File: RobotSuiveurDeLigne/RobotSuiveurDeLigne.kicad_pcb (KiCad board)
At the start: 2 copper layers, 108 x 48 mm, 22 parts, among them J1 US_IUT_VdA, J2 Conn_02x05_Odd_Even, U1 CNY70_IUT_VdA, U2 CNY70_IUT_VdA, U3 CNY70_IUT_VdA, U4 CNY70_IUT_VdA, U5 CNY70_IUT_VdA, U6 CNY70_IUT_VdA

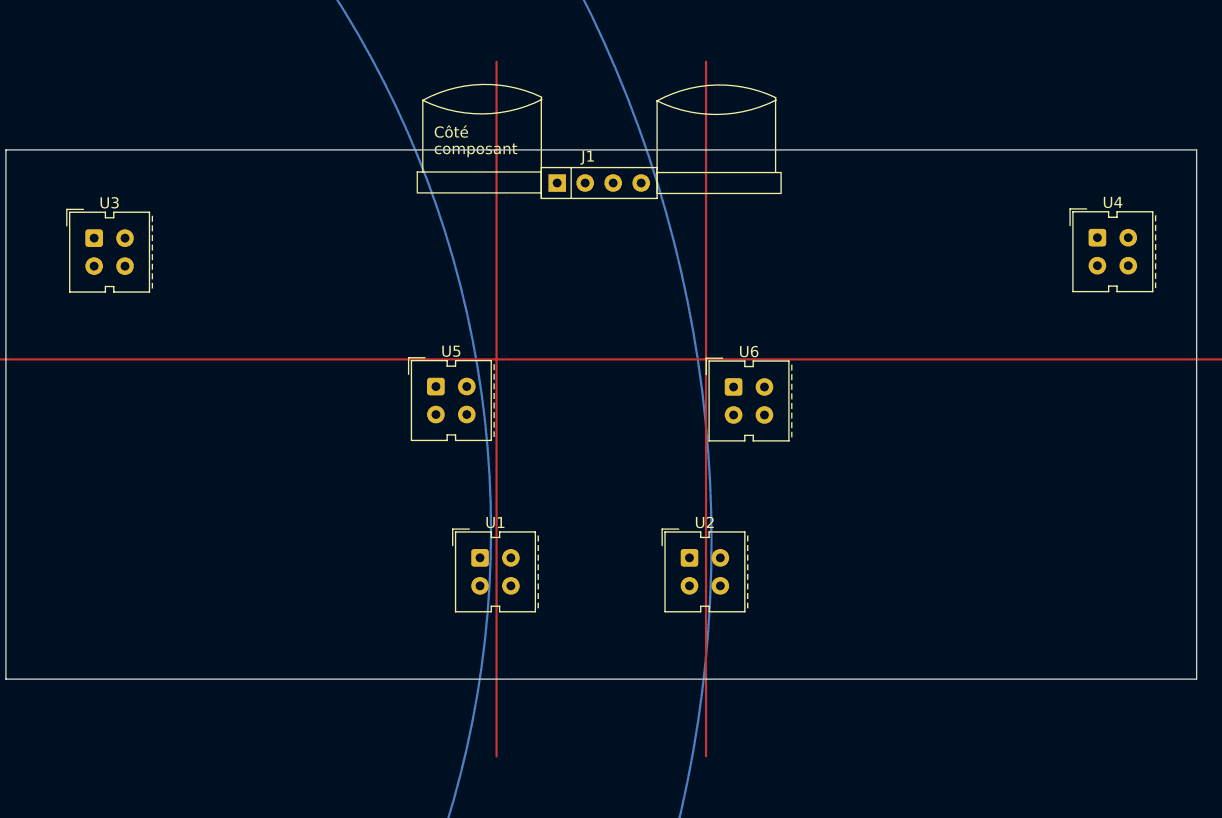
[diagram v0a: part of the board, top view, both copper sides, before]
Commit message: Routage V.1.2 G
Ajustements capteurs + ajout des trous de fixation
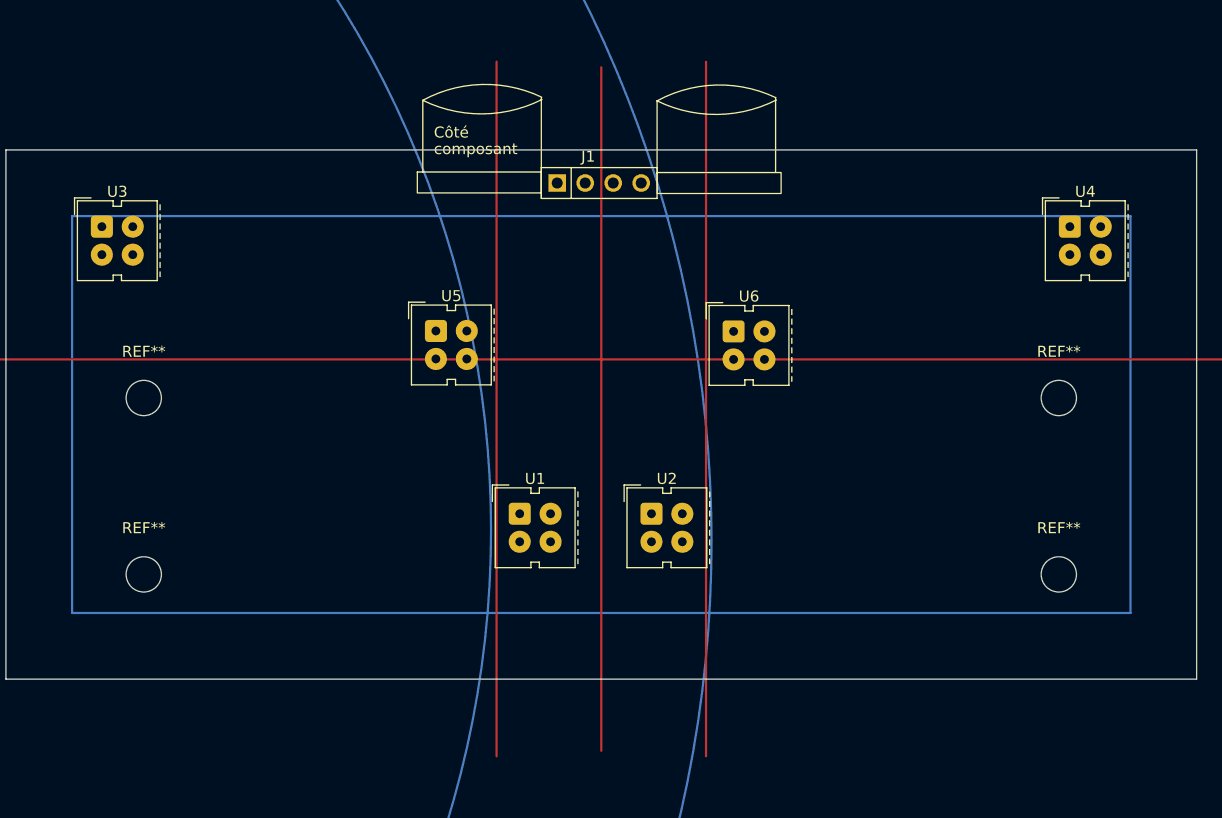
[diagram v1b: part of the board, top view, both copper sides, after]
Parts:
- added REF**: MountingHole_3.2mm_M3, MountingHole:MountingHole_3.2mm_M3, F.Cu at (185.5, 98.5)
- added REF**: MountingHole_3.2mm_M3, MountingHole:MountingHole_3.2mm_M3, F.Cu at (102.5, 98.5)
- added REF**: MountingHole_3.2mm_M3, MountingHole:MountingHole_3.2mm_M3, F.Cu at (185.5, 82.5)
- added REF**: MountingHole_3.2mm_M3, MountingHole:MountingHole_3.2mm_M3, F.Cu at (102.5, 82.5)
- moved U1 5.38 mm to (136.6, 93.0)
- moved U2 5.28 mm to (148.6, 93.0)
- moved U6 5.04 mm to (156.0, 76.5)
- moved U5 5.04 mm to (129.0, 76.4)
- moved U4 2.69 mm to (186.5, 67.0)
- moved U3 1.25 mm to (98.7, 67.0)

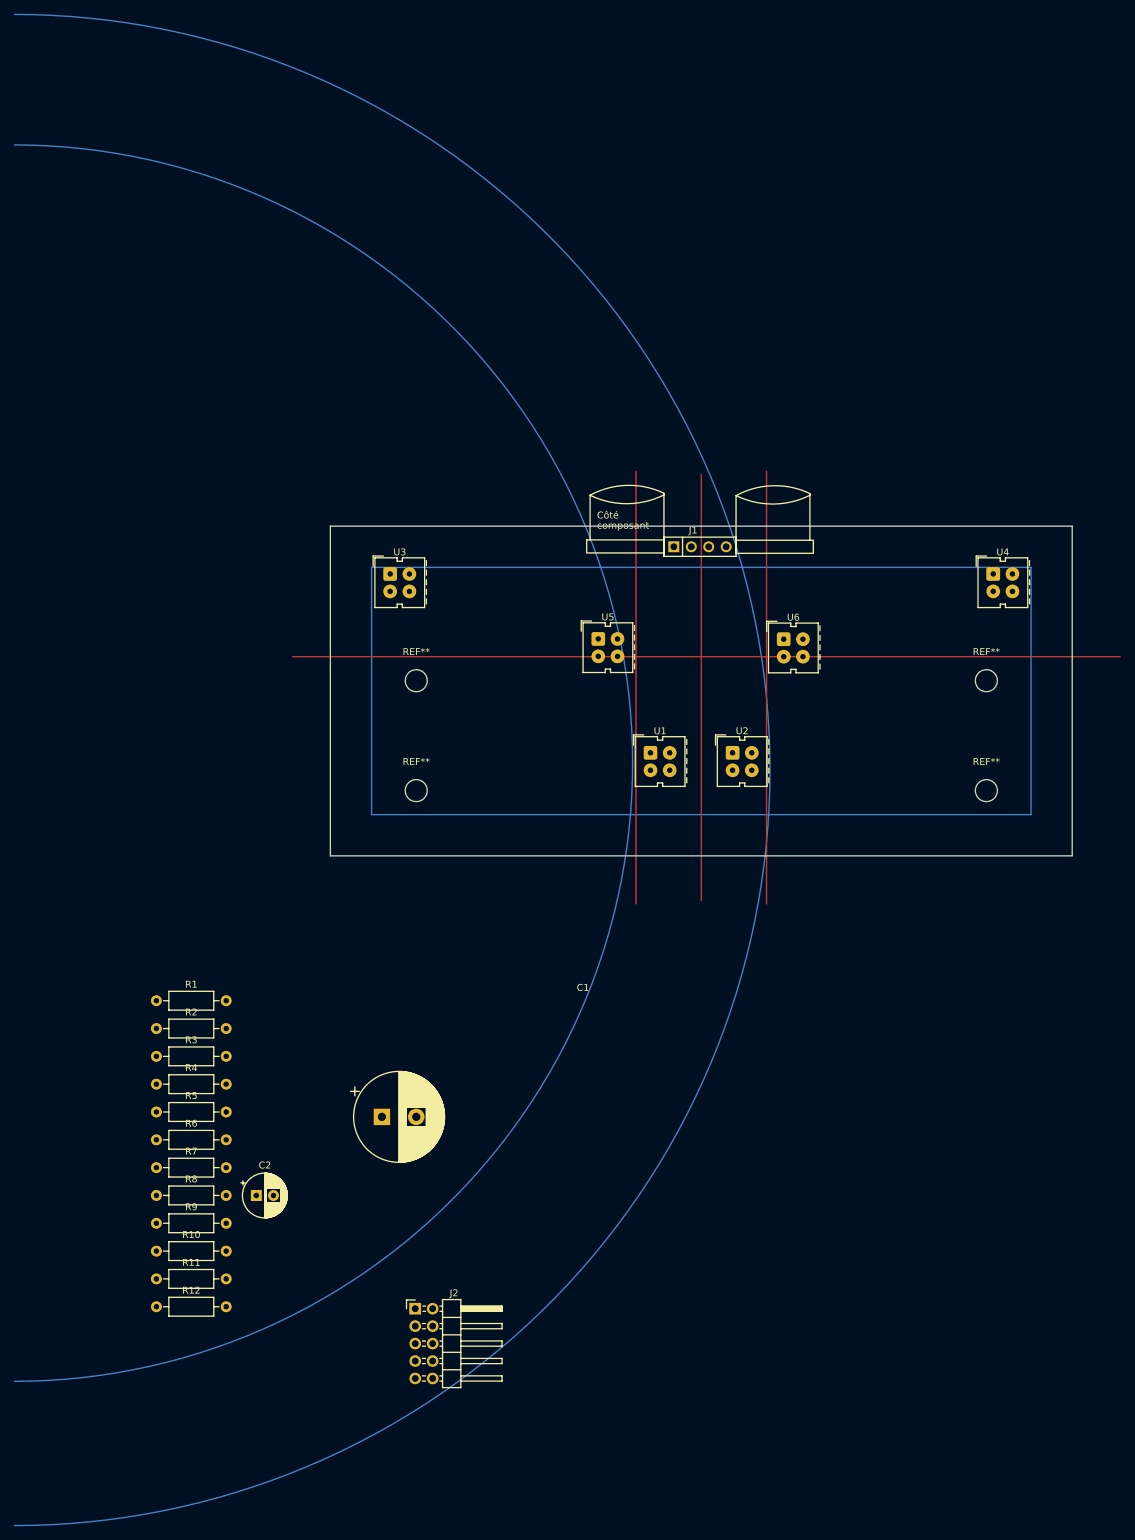
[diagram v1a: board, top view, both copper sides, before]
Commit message: ajouts et changements mineurs
ajout condensateur + résistances
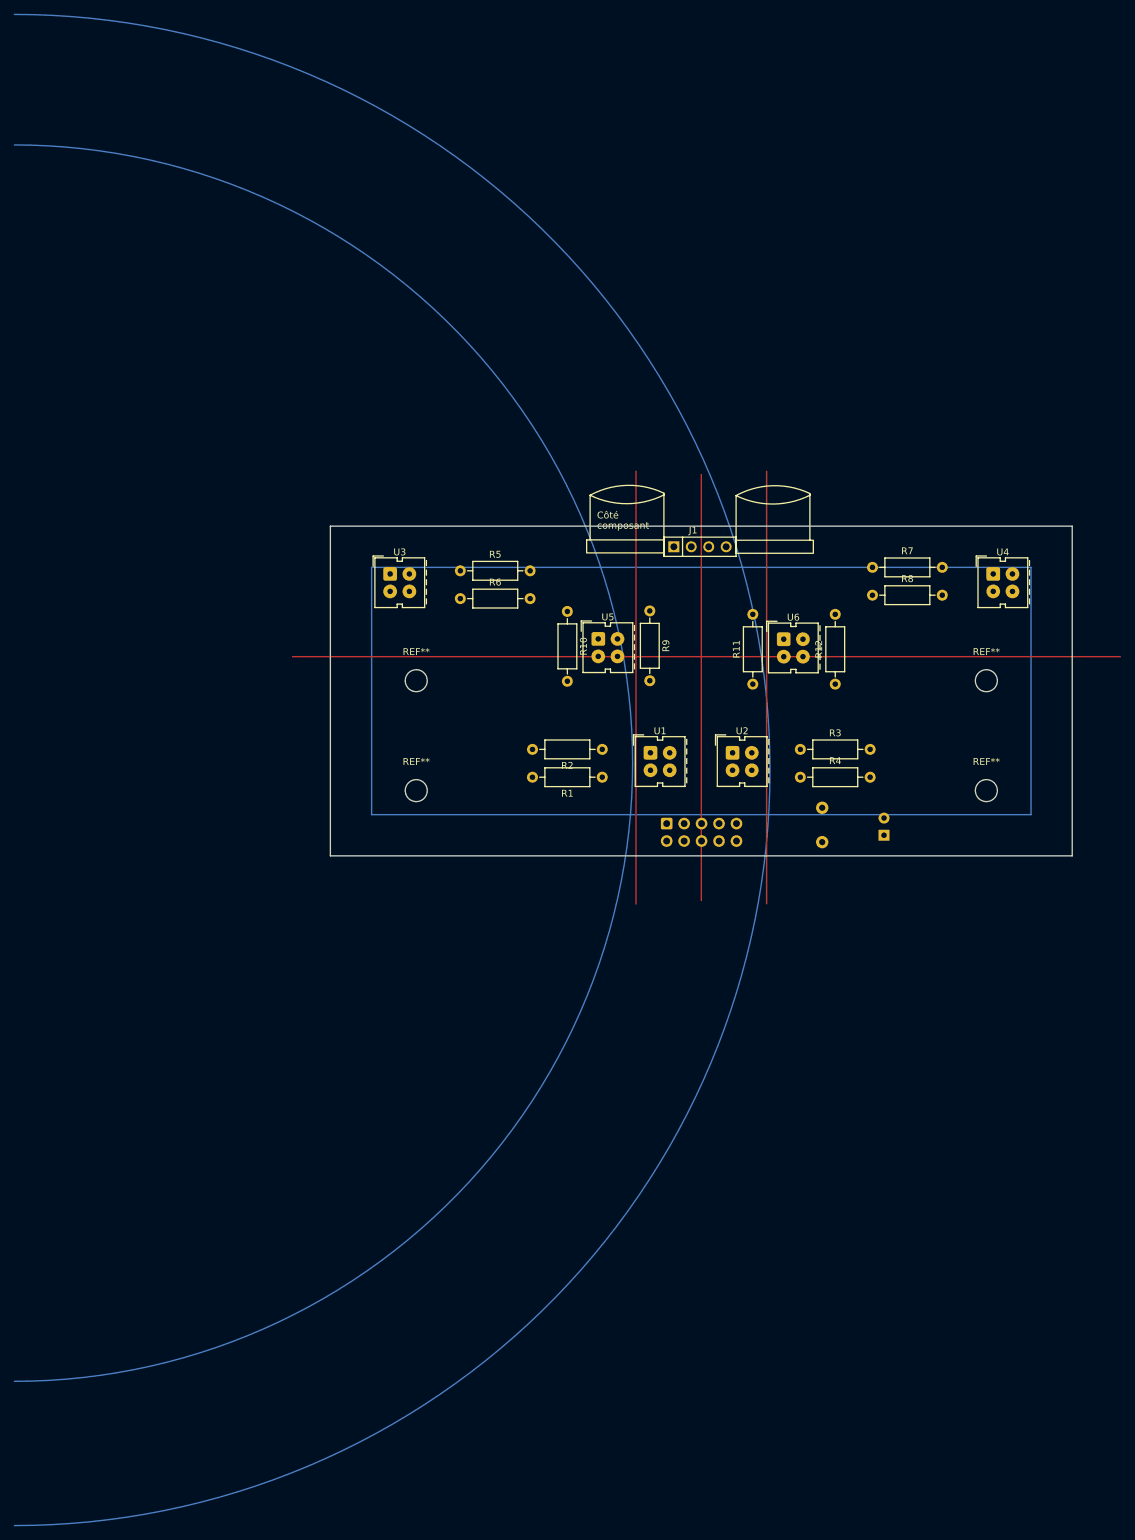
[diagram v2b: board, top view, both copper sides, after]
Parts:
- C1: footprint Capacitor_THT:CP_Radial_D13.0mm_P5.00mm -> Capacitor_THT:C_Rect_L7.0mm_W6.5mm_P5.00mm; moved to B.Cu
- C2: moved to B.Cu
- J2: footprint Connector_PinHeader_2.54mm:PinHeader_2x05_P2.54mm_Horizontal -> Connector_IDC:IDC-Header_2x05_P2.54mm_Horizontal; moved to B.Cu
- moved R7 136.0 mm to (168.9, 66.0)
- moved R8 136.0 mm to (168.9, 70.0)
- moved R12 134.1 mm to (163.5, 83.0), turned to 90 degrees
- moved R11 122.6 mm to (151.5, 83.0), turned to 90 degrees
- moved R9 114.5 mm to (136.5, 72.3), turned to -90 degrees
- moved R10 110.7 mm to (124.5, 72.4), turned to -90 degrees
- moved C2 105.4 mm to (170.6, 105.0), turned to 90 degrees
- moved R3 103.9 mm to (158.4, 92.5)
- moved R4 103.9 mm to (158.4, 96.5)
- moved R6 90.4 mm to (108.9, 70.5)
- moved R5 90.4 mm to (108.9, 66.5)
- moved J2 79.5 mm to (139.0, 103.3), turned to -90 degrees
- moved R2 76.6 mm to (129.6, 92.5), turned to 180 degrees
- moved C1 75.6 mm to (161.6, 106.0), turned to 90 degrees
- moved R1 72.6 mm to (129.6, 96.5), turned to 180 degrees

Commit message: 1ère version du routagge + changements mineurs
déplacements de résistances et rotation du capteur U5
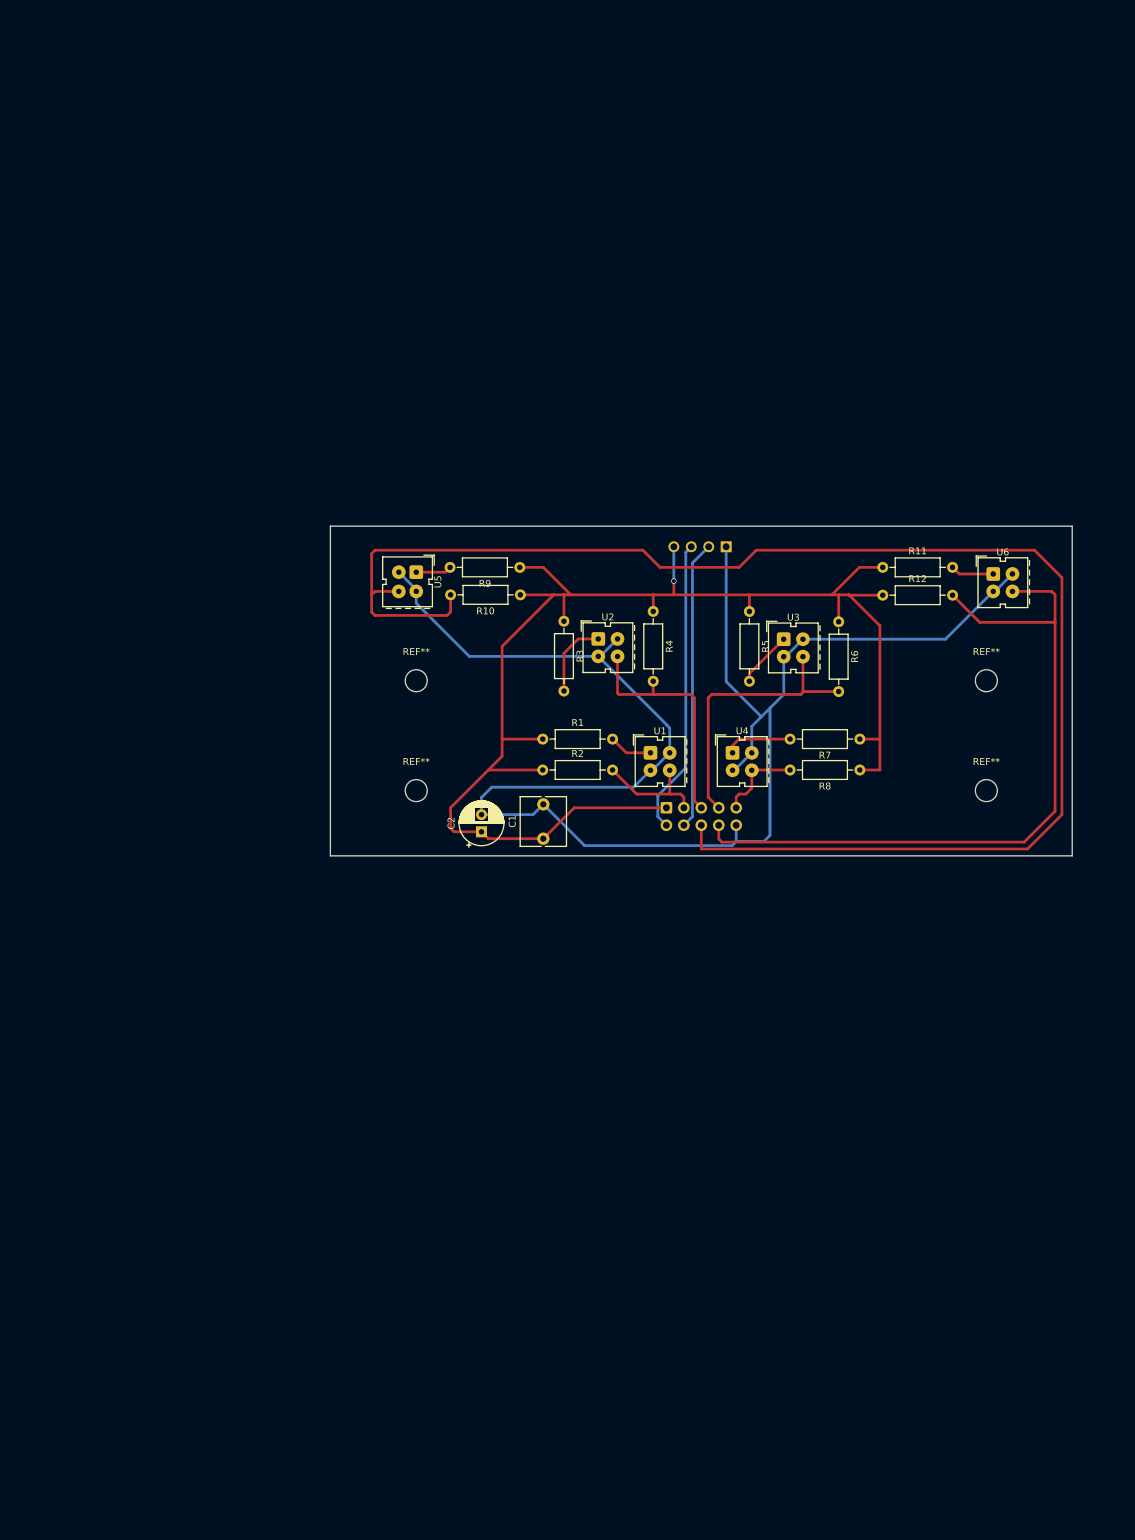
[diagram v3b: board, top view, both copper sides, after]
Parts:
- C1, C2: moved to F.Cu
- J1: moved to B.Cu
- moved C2 58.6 mm to (112.0, 104.5)
- moved U3 58.1 mm to (156.0, 76.5)
- moved R6 55.2 mm to (164.0, 73.9), turned to -90 degrees
- moved U4 46.0 mm to (148.6, 93.0)
- moved R5 42.5 mm to (151.0, 72.4), turned to -90 degrees
- moved C1 40.6 mm to (121.0, 105.5)
- moved R3 39.2 mm to (124.0, 73.8), turned to -90 degrees
- moved R4 32.3 mm to (137.0, 72.4), turned to -90 degrees
- moved U6 31.9 mm to (186.5, 67.0)
- moved U5 28.2 mm to (102.5, 66.7), turned to -90 degrees
- moved U2 25.6 mm to (129.0, 76.4)
- moved R8 25.5 mm to (167.1, 95.5), turned to 180 degrees
- moved R11 25.4 mm to (170.4, 66.0), turned to 0 degrees
- moved R7 25.1 mm to (167.1, 91.0), turned to 180 degrees
- moved R9 20.0 mm to (117.6, 66.0), turned to 180 degrees
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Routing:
- net GND: track 0.00 -> 243.2 mm
- net /D0: track 0.00 -> 224.3 mm
- net VCC: track 0.00 -> 211.7 mm, vias 0 -> 1
- net /D1: track 0.00 -> 107.5 mm
- net Net-(J2-Pin_2): track 0.00 -> 43.1 mm
- net Net-(J2-Pin_4): track 0.00 -> 42.0 mm
- net /AN2: track 0.00 -> 41.2 mm
- net /AN1: track 0.00 -> 35.2 mm
- net /AN0: track 0.00 -> 17.1 mm
- net /AN3: track 0.00 -> 12.6 mm
- net Net-(U2-A): track 0.00 -> 11.4 mm
- net Net-(U4-A): track 0.00 -> 9.81 mm
- net Net-(U3-A): track 0.00 -> 8.19 mm
- net Net-(U1-A): track 0.00 -> 6.35 mm
- net Net-(U6-A): track 0.00 -> 6.32 mm
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
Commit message: GND retravaillé
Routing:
- net GND: track 243.2 -> 3.12 mm
- net Net-(J2-Pin_4): track 42.0 -> 58.5 mm
- net Net-(J2-Pin_2): track 43.1 -> 48.4 mm
- net VCC: track 211.7 -> 215.4 mm, vias 1 -> 0
- added copper zone on B.Cu, net GND
- added copper zone on F.Cu, net GND
